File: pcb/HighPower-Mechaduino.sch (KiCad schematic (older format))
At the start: 51 parts, among them J1 SUPPLY, J2 STEPPER, P1 SWD, P4 -, P5 -, P6 -, P7 -, Q1 SSM3J328R, Q2 BSS138, SW1 SW_PUSH, U1 AS5047D, U2 AP2112K-3.3TRG1, U3 AT24CS64-SSHM

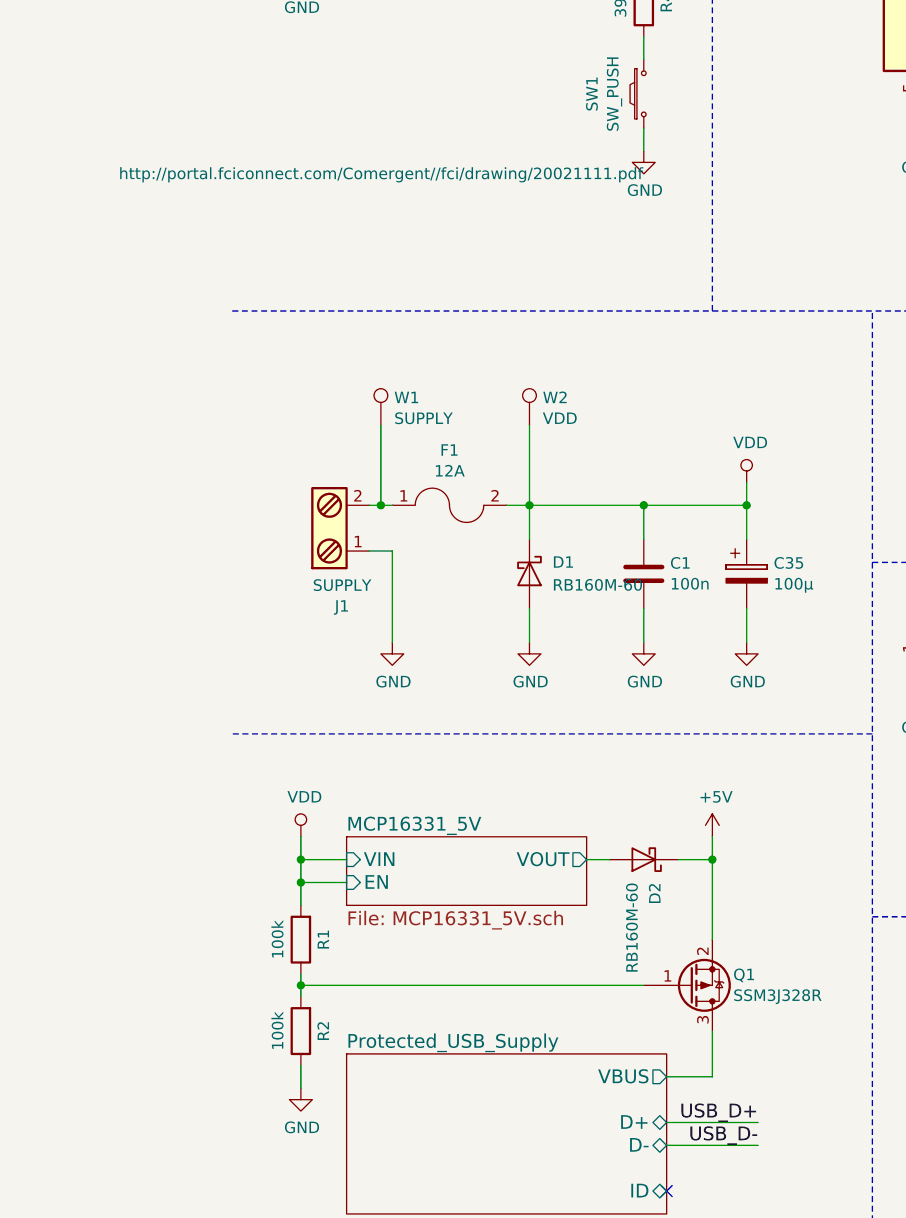
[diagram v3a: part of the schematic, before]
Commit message: Add more BOM informations
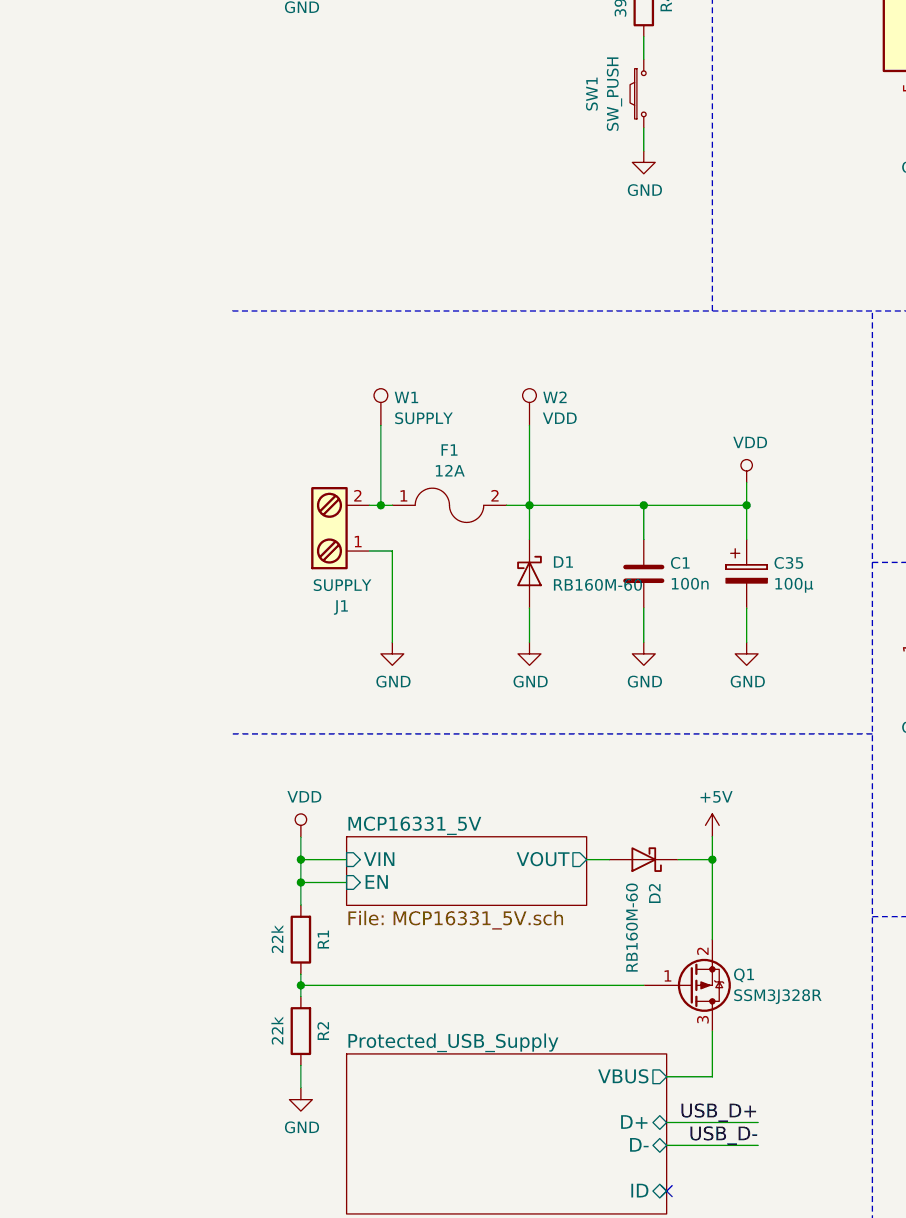
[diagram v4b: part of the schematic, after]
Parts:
- C1, C2, C3, C4, C5, C6, C7, C8: Digi-Key Minimum Quantity (none) -> 1; Digi-Key Part Number (none) -> 311-1343-1-ND
- C35: Digi-Key Minimum Quantity (none) -> 1; Digi-Key Part Number (none) -> 493-7453-1-ND
- R1: value 100k -> 22k; Digi-Key Minimum Quantity (none) -> 5000; Digi-Key Part Number (none) -> 311-22.0KHRTR-ND
- R10, R9: Digi-Key Minimum Quantity (none) -> 5000; Digi-Key Part Number (none) -> 311-1.00KHRTR-ND
- R2: value 100k -> 22k
- R23, R24, R7, R8: Digi-Key Minimum Quantity (none) -> 5000; Digi-Key Part Number (none) -> 311-4.70KHRTR-ND
- R3, R5: Digi-Key Minimum Quantity (none) -> 5000; Digi-Key Part Number (none) -> 311-22.0KHRTR-ND
- R4: Digi-Key Minimum Quantity (none) -> 5000; Digi-Key Part Number (none) -> 311-39GRTR-ND
- R6: Digi-Key Minimum Quantity (none) -> 5000; Digi-Key Part Number (none) -> 311-330GRTR-ND
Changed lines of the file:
@@
 F 2 "Capacitors_SMD:C_0603" H 4138 1150 50  0001 C CNN
 F 3 "" H 4100 1300 50  0000 C CNN
+F 4 "311-1343-1-ND" H 4100 1300 60  0001 C CNN "Digi-Key Part Number"
+F 5 "1" H 4100 1300 60  0001 C CNN "Digi-Key Minimum Quantity"
 	1    4100 1300
 	0    1    1    0
@@
 F 2 "Capacitors_SMD:C_0603" H 3488 1150 50  0001 C CNN
 F 3 "" H 3450 1300 50  0000 C CNN
+F 4 "311-1343-1-ND" H 3450 1300 60  0001 C CNN "Digi-Key Part Number"
+F 5 "1" H 3450 1300 60  0001 C CNN "Digi-Key Minimum Quantity"
 	1    3450 1300
 	0    1    1    0
@@
 F 2 "Resistors_SMD:R_0603" V 7530 1500 50  0001 C CNN
 F 3 "" H 7600 1500 50  0000 C CNN
+F 4 "311-4.70KHRTR-ND" H 7600 1500 60  0001 C CNN "Digi-Key Part Number"
+F 5 "5000" H 7600 1500 60  0001 C CNN "Digi-Key Minimum Quantity"
 	1    7600 1500
 	0    1    1    0
@@
 F 2 "Resistors_SMD:R_0603" V 7530 2800 50  0001 C CNN
 F 3 "" H 7600 2800 50  0000 C CNN
+F 4 "311-4.70KHRTR-ND" H 7600 2800 60  0001 C CNN "Digi-Key Part Number"
+F 5 "5000" H 7600 2800 60  0001 C CNN "Digi-Key Minimum Quantity"
 	1    7600 2800
 	0    1    1    0
@@
 F 2 "Capacitors_SMD:C_0603" H 8288 1600 50  0001 C CNN
 F 3 "" H 8250 1750 50  0000 C CNN
+F 4 "311-1343-1-ND" H 8250 1750 60  0001 C CNN "Digi-Key Part Number"
+F 5 "1" H 8250 1750 60  0001 C CNN "Digi-Key Minimum Quantity"
 	1    8250 1750
 	-1   0    0    1
@@
 F 2 "Capacitors_SMD:C_0603" H 8288 2900 50  0001 C CNN
 F 3 "" H 8250 3050 50  0000 C CNN
+F 4 "311-1343-1-ND" H 8250 3050 60  0001 C CNN "Digi-Key Part Number"
+F 5 "1" H 8250 3050 60  0001 C CNN "Digi-Key Minimum Quantity"
 	1    8250 3050
 	-1   0    0    1
@@
 F 2 "Resistors_SMD:R_0603" V 7880 1750 50  0001 C CNN
 F 3 "" H 7950 1750 50  0000 C CNN
+F 4 "311-1.00KHRTR-ND" H 7950 1750 60  0001 C CNN "Digi-Key Part Number"
+F 5 "5000" H 7950 1750 60  0001 C CNN "Digi-Key Minimum Quantity"
 	1    7950 1750
 	-1   0    0    1
@@
 F 2 "Resistors_SMD:R_0603" V 7880 3050 50  0001 C CNN
 F 3 "" H 7950 3050 50  0000 C CNN
+F 4 "311-1.00KHRTR-ND" H 7950 3050 60  0001 C CNN "Digi-Key Part Number"
+F 5 "5000" H 7950 3050 60  0001 C CNN "Digi-Key Minimum Quantity"
 	1    7950 3050
 	-1   0    0    1
@@
 F 2 "Capacitors_SMD:C_0603" H 2338 4600 50  0001 C CNN
 F 3 "" H 2300 4750 50  0000 C CNN
+F 4 "311-1343-1-ND" H 2300 4750 60  0001 C CNN "Digi-Key Part Number"
+F 5 "1" H 2300 4750 60  0001 C CNN "Digi-Key Minimum Quantity"
 	1    2300 4750
 	-1   0    0    1
@@
 F 1 "SWD" H 1150 2124 50  0000 C CNN
 F 2 "Pin_Headers:Pin_Header_Straight_2x05_Pitch1.27mm" H 1150 600 50  0001 C CNN
-F 3 "http://portal.fciconnect.com/Comergent//fci/drawing/20021111.pdf" H 1150 600 50  0000 C CNN
+F 3 "http://portal.fciconnect.com/Comergent//fci/drawing/20021111.pdf" H 1150 600 50  0001 C CNN
 F 4 "609-3712-ND" H 1150 1800 60  0001 C CNN "Digi-Key Part Number"
 F 5 "1" H 1150 1800 60  0001 C CNN "Digi-Key Minimum Quantity"
@@
 F 2 "Resistors_SMD:R_0603" V 2230 2250 50  0001 C CNN
 F 3 "" H 2300 2250 50  0000 C CNN
+F 4 "311-39GRTR-ND" H 2300 2250 60  0001 C CNN "Digi-Key Part Number"
+F 5 "5000" H 2300 2250 60  0001 C CNN "Digi-Key Minimum Quantity"
 	1    2300 2250
 	-1   0    0    1
@@
 F 2 "Resistors_SMD:R_0603" V 2230 1700 50  0001 C CNN
 F 3 "" H 2300 1700 50  0000 C CNN
+F 4 "311-22.0KHRTR-ND" H 2300 1700 60  0001 C CNN "Digi-Key Part Number"
+F 5 "5000" H 2300 1700 60  0001 C CNN "Digi-Key Minimum Quantity"
 	1    2300 1700
 	-1   0    0    1
@@
 F 2 "Resistors_SMD:R_0603" V 5430 2750 50  0001 C CNN
 F 3 "" H 5500 2750 50  0000 C CNN
+F 4 "311-22.0KHRTR-ND" H 5500 2750 60  0001 C CNN "Digi-Key Part Number"
+F 5 "5000" H 5500 2750 60  0001 C CNN "Digi-Key Minimum Quantity"
 	1    5500 2750
 	-1   0    0    1
@@
 F 2 "Resistors_SMD:R_0603" V 5830 2000 50  0001 C CNN
 F 3 "" H 5900 2000 50  0000 C CNN
+F 4 "311-330GRTR-ND" H 5900 2000 60  0001 C CNN "Digi-Key Part Number"
+F 5 "5000" H 5900 2000 60  0001 C CNN "Digi-Key Minimum Quantity"
 	1    5900 2000
 	-1   0    0    1
@@
 P 800 6350
 F 0 "R1" V 700 6350 50  0000 C CNN
-F 1 "100k" V 900 6350 50  0000 C CNN
+F 1 "22k" V 900 6350 50  0000 C CNN
 F 2 "Resistors_SMD:R_0603" V 730 6350 50  0001 C CNN
 F 3 "" H 800 6350 50  0000 C CNN
+F 4 "311-22.0KHRTR-ND" H 800 6350 60  0001 C CNN "Digi-Key Part Number"
+F 5 "5000" H 800 6350 60  0001 C CNN "Digi-Key Minimum Quantity"
 	1    800  6350
 	-1   0    0    1
@@
 P 800 6750
 F 0 "R2" V 700 6750 50  0000 C CNN
-F 1 "100k" V 900 6750 50  0000 C CNN
+F 1 "22k" V 900 6750 50  0000 C CNN
 F 2 "Resistors_SMD:R_0603" V 730 6750 50  0001 C CNN
 F 3 "" H 800 6750 50  0000 C CNN
@@
 F 2 "Capacitors_SMD:C_0603" H 5488 6900 50  0001 C CNN
 F 3 "" H 5450 7050 50  0000 C CNN
+F 4 "311-1343-1-ND" H 5450 7050 60  0001 C CNN "Digi-Key Part Number"
+F 5 "1" H 5450 7050 60  0001 C CNN "Digi-Key Minimum Quantity"
 	1    5450 7050
 	-1   0    0    1
@@
 F 2 "Capacitors_SMD:C_0603" H 3688 7050 50  0001 C CNN
 F 3 "" H 3650 7200 50  0000 C CNN
+F 4 "311-1343-1-ND" H 3650 7200 60  0001 C CNN "Digi-Key Part Number"
+F 5 "1" H 3650 7200 60  0001 C CNN "Digi-Key Minimum Quantity"
 	1    3650 7200
 	-1   0    0    1
@@
 F 2 "Capacitors_SMD:C_0603" H 4888 7050 50  0001 C CNN
 F 3 "" H 4850 7200 50  0000 C CNN
+F 4 "311-1343-1-ND" H 4850 7200 60  0001 C CNN "Digi-Key Part Number"
+F 5 "1" H 4850 7200 60  0001 C CNN "Digi-Key Minimum Quantity"
 	1    4850 7200
 	-1   0    0    1
@@
 F 2 "Capacitors_SMD:c_elec_10x10" H 2788 4600 50  0001 C CNN
 F 3 "" H 2750 4750 50  0000 C CNN
+F 4 "493-7453-1-ND" H 2750 4750 60  0001 C CNN "Digi-Key Part Number"
+F 5 "1" H 2750 4750 60  0001 C CNN "Digi-Key Minimum Quantity"
 	1    2750 4750
 	1    0    0    -1
@@
 F 2 "Resistors_SMD:R_0603" V 10780 3950 50  0001 C CNN
 F 3 "" H 10850 3950 50  0000 C CNN
+F 4 "311-4.70KHRTR-ND" H 10850 3950 60  0001 C CNN "Digi-Key Part Number"
+F 5 "5000" H 10850 3950 60  0001 C CNN "Digi-Key Minimum Quantity"
 	1    10850 3950
 	-1   0    0    1
@@
 F 2 "Resistors_SMD:R_0603" V 10980 3950 50  0001 C CNN
 F 3 "" H 11050 3950 50  0000 C CNN
+F 4 "311-4.70KHRTR-ND" H 11050 3950 60  0001 C CNN "Digi-Key Part Number"
+F 5 "5000" H 11050 3950 60  0001 C CNN "Digi-Key Minimum Quantity"
 	1    11050 3950
 	-1   0    0    1

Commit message: Improve BOM
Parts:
- R1, R3, R5: Digi-Key Minimum Quantity 5000 -> 1; Digi-Key Part Number 311-22.0KHRTR-ND -> 311-22.0KHRCT-ND
- R10, R9: Digi-Key Minimum Quantity 5000 -> 1; Digi-Key Part Number 311-1.00KHRTR-ND -> 311-1.00KHRCT-ND
- R2: Digi-Key Minimum Quantity (none) -> 1; Digi-Key Part Number (none) -> 311-22.0KHRCT-ND
- R23, R24, R7, R8: Digi-Key Minimum Quantity 5000 -> 1; Digi-Key Part Number 311-4.70KHRTR-ND -> 311-4.70KHRCT-ND
- R4: Digi-Key Minimum Quantity 5000 -> 1; Digi-Key Part Number 311-39GRTR-ND -> 311-39GRCT-ND
- R6: Digi-Key Minimum Quantity 5000 -> 1; Digi-Key Part Number 311-330GRTR-ND -> 311-330GRCT-ND
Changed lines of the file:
@@
 F 2 "Resistors_SMD:R_0603" V 7530 1500 50  0001 C CNN
 F 3 "" H 7600 1500 50  0000 C CNN
-F 4 "311-4.70KHRTR-ND" H 7600 1500 60  0001 C CNN "Digi-Key Part Number"
-F 5 "5000" H 7600 1500 60  0001 C CNN "Digi-Key Minimum Quantity"
+F 4 "311-4.70KHRCT-ND" H 7600 1500 60  0001 C CNN "Digi-Key Part Number"
+F 5 "1" H 7600 1500 60  0001 C CNN "Digi-Key Minimum Quantity"
 	1    7600 1500
 	0    1    1    0
@@
 F 2 "Resistors_SMD:R_0603" V 7530 2800 50  0001 C CNN
 F 3 "" H 7600 2800 50  0000 C CNN
-F 4 "311-4.70KHRTR-ND" H 7600 2800 60  0001 C CNN "Digi-Key Part Number"
-F 5 "5000" H 7600 2800 60  0001 C CNN "Digi-Key Minimum Quantity"
+F 4 "311-4.70KHRCT-ND" H 7600 2800 60  0001 C CNN "Digi-Key Part Number"
+F 5 "1" H 7600 2800 60  0001 C CNN "Digi-Key Minimum Quantity"
 	1    7600 2800
 	0    1    1    0
@@
 F 2 "Resistors_SMD:R_0603" V 7880 1750 50  0001 C CNN
 F 3 "" H 7950 1750 50  0000 C CNN
-F 4 "311-1.00KHRTR-ND" H 7950 1750 60  0001 C CNN "Digi-Key Part Number"
-F 5 "5000" H 7950 1750 60  0001 C CNN "Digi-Key Minimum Quantity"
+F 4 "311-1.00KHRCT-ND" H 7950 1750 60  0001 C CNN "Digi-Key Part Number"
+F 5 "1" H 7950 1750 60  0001 C CNN "Digi-Key Minimum Quantity"
 	1    7950 1750
 	-1   0    0    1
@@
 F 2 "Resistors_SMD:R_0603" V 7880 3050 50  0001 C CNN
 F 3 "" H 7950 3050 50  0000 C CNN
-F 4 "311-1.00KHRTR-ND" H 7950 3050 60  0001 C CNN "Digi-Key Part Number"
-F 5 "5000" H 7950 3050 60  0001 C CNN "Digi-Key Minimum Quantity"
+F 4 "311-1.00KHRCT-ND" H 7950 3050 60  0001 C CNN "Digi-Key Part Number"
+F 5 "1" H 7950 3050 60  0001 C CNN "Digi-Key Minimum Quantity"
 	1    7950 3050
 	-1   0    0    1
@@
 F 2 "Resistors_SMD:R_0603" V 2230 2250 50  0001 C CNN
 F 3 "" H 2300 2250 50  0000 C CNN
-F 4 "311-39GRTR-ND" H 2300 2250 60  0001 C CNN "Digi-Key Part Number"
-F 5 "5000" H 2300 2250 60  0001 C CNN "Digi-Key Minimum Quantity"
+F 4 "311-39GRCT-ND" H 2300 2250 60  0001 C CNN "Digi-Key Part Number"
+F 5 "1" H 2300 2250 60  0001 C CNN "Digi-Key Minimum Quantity"
 	1    2300 2250
 	-1   0    0    1
@@
 F 2 "Resistors_SMD:R_0603" V 2230 1700 50  0001 C CNN
 F 3 "" H 2300 1700 50  0000 C CNN
-F 4 "311-22.0KHRTR-ND" H 2300 1700 60  0001 C CNN "Digi-Key Part Number"
-F 5 "5000" H 2300 1700 60  0001 C CNN "Digi-Key Minimum Quantity"
+F 4 "311-22.0KHRCT-ND" H 2300 1700 60  0001 C CNN "Digi-Key Part Number"
+F 5 "1" H 2300 1700 60  0001 C CNN "Digi-Key Minimum Quantity"
 	1    2300 1700
 	-1   0    0    1
@@
 F 2 "Resistors_SMD:R_0603" V 5430 2750 50  0001 C CNN
 F 3 "" H 5500 2750 50  0000 C CNN
-F 4 "311-22.0KHRTR-ND" H 5500 2750 60  0001 C CNN "Digi-Key Part Number"
-F 5 "5000" H 5500 2750 60  0001 C CNN "Digi-Key Minimum Quantity"
+F 4 "311-22.0KHRCT-ND" H 5500 2750 60  0001 C CNN "Digi-Key Part Number"
+F 5 "1" H 5500 2750 60  0001 C CNN "Digi-Key Minimum Quantity"
 	1    5500 2750
 	-1   0    0    1
@@
 F 2 "Resistors_SMD:R_0603" V 5830 2000 50  0001 C CNN
 F 3 "" H 5900 2000 50  0000 C CNN
-F 4 "311-330GRTR-ND" H 5900 2000 60  0001 C CNN "Digi-Key Part Number"
-F 5 "5000" H 5900 2000 60  0001 C CNN "Digi-Key Minimum Quantity"
+F 4 "311-330GRCT-ND" H 5900 2000 60  0001 C CNN "Digi-Key Part Number"
+F 5 "1" H 5900 2000 60  0001 C CNN "Digi-Key Minimum Quantity"
 	1    5900 2000
 	-1   0    0    1
@@
 F 2 "Resistors_SMD:R_0603" V 730 6350 50  0001 C CNN
 F 3 "" H 800 6350 50  0000 C CNN
-F 4 "311-22.0KHRTR-ND" H 800 6350 60  0001 C CNN "Digi-Key Part Number"
-F 5 "5000" H 800 6350 60  0001 C CNN "Digi-Key Minimum Quantity"
+F 4 "311-22.0KHRCT-ND" H 800 6350 60  0001 C CNN "Digi-Key Part Number"
+F 5 "1" H 800 6350 60  0001 C CNN "Digi-Key Minimum Quantity"
 	1    800  6350
 	-1   0    0    1
@@
 F 2 "Resistors_SMD:R_0603" V 730 6750 50  0001 C CNN
 F 3 "" H 800 6750 50  0000 C CNN
+F 4 "311-22.0KHRCT-ND" H 800 6750 60  0001 C CNN "Digi-Key Part Number"
+F 5 "1" H 800 6750 60  0001 C CNN "Digi-Key Minimum Quantity"
 	1    800  6750
 	-1   0    0    1
@@
 F 2 "Resistors_SMD:R_0603" V 10780 3950 50  0001 C CNN
 F 3 "" H 10850 3950 50  0000 C CNN
-F 4 "311-4.70KHRTR-ND" H 10850 3950 60  0001 C CNN "Digi-Key Part Number"
-F 5 "5000" H 10850 3950 60  0001 C CNN "Digi-Key Minimum Quantity"
+F 4 "311-4.70KHRCT-ND" H 10850 3950 60  0001 C CNN "Digi-Key Part Number"
+F 5 "1" H 10850 3950 60  0001 C CNN "Digi-Key Minimum Quantity"
 	1    10850 3950
 	-1   0    0    1
@@
 F 2 "Resistors_SMD:R_0603" V 10980 3950 50  0001 C CNN
 F 3 "" H 11050 3950 50  0000 C CNN
-F 4 "311-4.70KHRTR-ND" H 11050 3950 60  0001 C CNN "Digi-Key Part Number"
-F 5 "5000" H 11050 3950 60  0001 C CNN "Digi-Key Minimum Quantity"
+F 4 "311-4.70KHRCT-ND" H 11050 3950 60  0001 C CNN "Digi-Key Part Number"
+F 5 "1" H 11050 3950 60  0001 C CNN "Digi-Key Minimum Quantity"
 	1    11050 3950
 	-1   0    0    1
